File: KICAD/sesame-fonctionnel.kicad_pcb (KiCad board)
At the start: 2 copper layers, 1 part

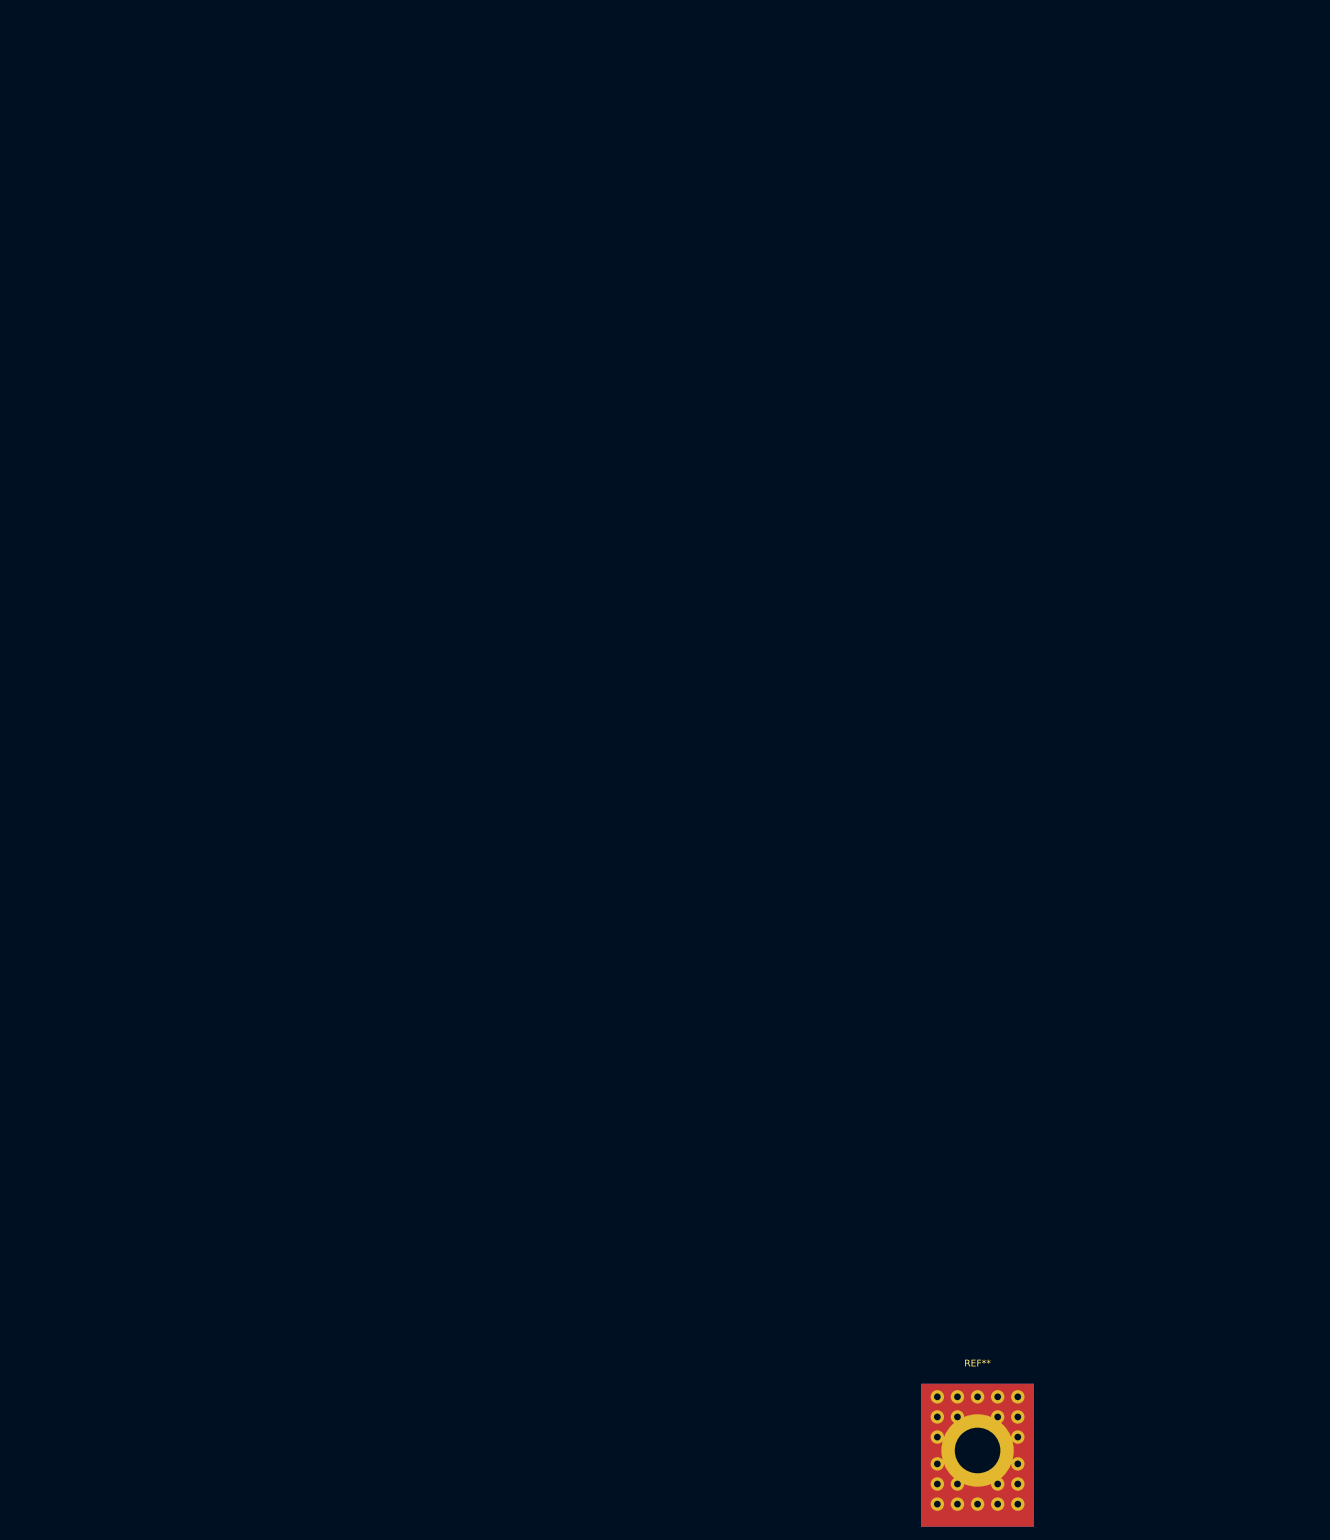
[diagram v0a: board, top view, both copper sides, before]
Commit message: edit footprints by jmt
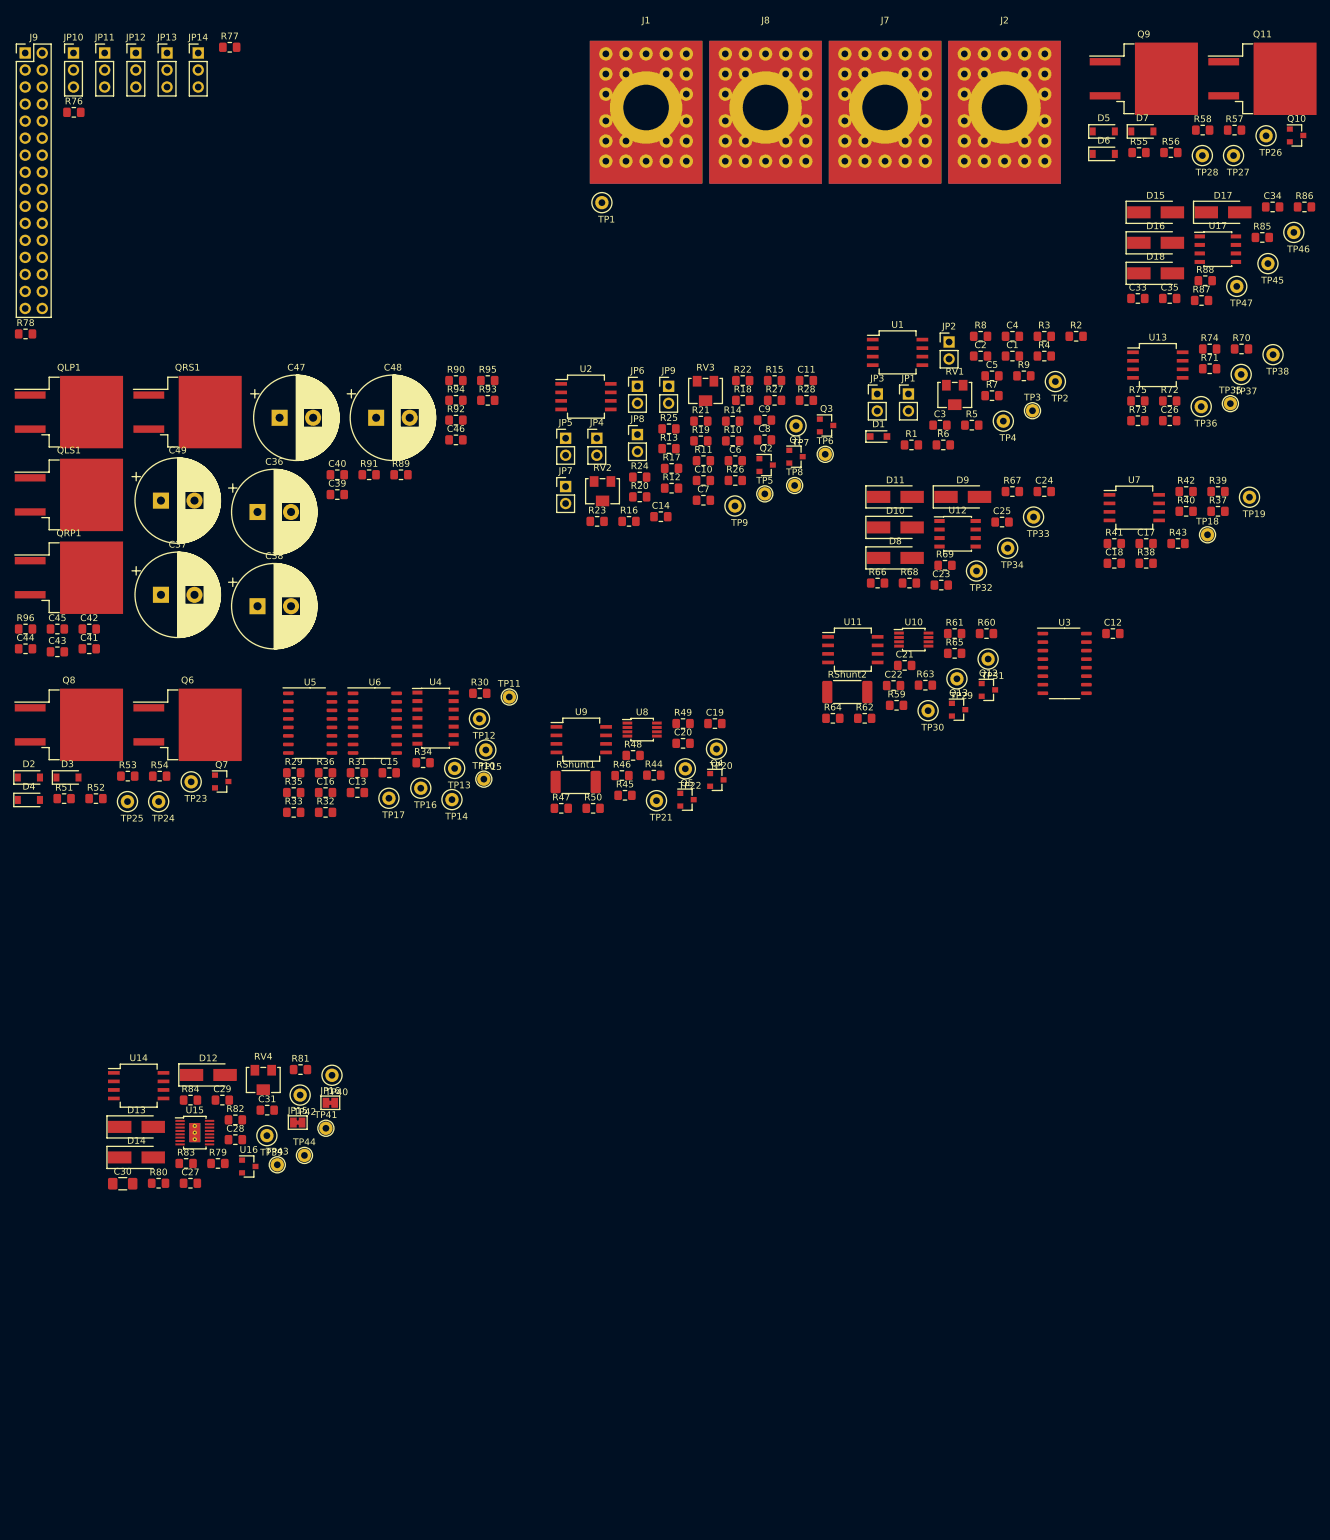
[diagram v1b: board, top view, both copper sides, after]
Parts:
- removed REF**: CXS70-14-C, Sesame_footprint:CXS70-14-C
- added C1: 100n, Capacitor_SMD:C_0805_2012Metric_Pad1.15x1.40mm_HandSolder, F.Cu at (160.8, -69.9)
- added C10: 10n, Capacitor_SMD:C_0805_2012Metric_Pad1.15x1.40mm_HandSolder, F.Cu at (114.7, -51.4)
- added C11: 10n, Capacitor_SMD:C_0805_2012Metric_Pad1.15x1.40mm_HandSolder, F.Cu at (130.1, -66.2)
- added C12: 100n, Capacitor_SMD:C_0805_2012Metric_Pad1.15x1.40mm_HandSolder, F.Cu at (175.8, -28.5)
- added C13: 100n, Capacitor_SMD:C_0805_2012Metric_Pad1.15x1.40mm_HandSolder, F.Cu at (63.1, -4.81)
- added C14: 100n, Capacitor_SMD:C_0805_2012Metric_Pad1.15x1.40mm_HandSolder, F.Cu at (108.4, -46.0)
- added C15: 100n, Capacitor_SMD:C_0805_2012Metric_Pad1.15x1.40mm_HandSolder, F.Cu at (67.9, -7.76)
- added C16: 100n, Capacitor_SMD:C_0805_2012Metric_Pad1.15x1.40mm_HandSolder, F.Cu at (58.4, -4.81)
- added C17: 100n, Capacitor_SMD:C_0805_2012Metric_Pad1.15x1.40mm_HandSolder, F.Cu at (180.7, -42.0)
- added C18: 2.2n, Capacitor_SMD:C_0805_2012Metric_Pad1.15x1.40mm_HandSolder, F.Cu at (176.0, -39.0)
- added C19: 100n, Capacitor_SMD:C_0805_2012Metric_Pad1.15x1.40mm_HandSolder, F.Cu at (116.4, -15.1)
- added C2: NC, Capacitor_SMD:C_0805_2012Metric_Pad1.15x1.40mm_HandSolder, F.Cu at (156.1, -69.9)
- added C20: 100n, Capacitor_SMD:C_0805_2012Metric_Pad1.15x1.40mm_HandSolder, F.Cu at (111.7, -12.2)
- added C21: 100n, Capacitor_SMD:C_0805_2012Metric_Pad1.15x1.40mm_HandSolder, F.Cu at (144.7, -23.8)
- added C22: 100n, Capacitor_SMD:C_0805_2012Metric_Pad1.15x1.40mm_HandSolder, F.Cu at (143.1, -20.8)
- added C23: 100n, Capacitor_SMD:C_0805_2012Metric_Pad1.15x1.40mm_HandSolder, F.Cu at (150.2, -35.8)
- added C24: 100n, Capacitor_SMD:C_0805_2012Metric_Pad1.15x1.40mm_HandSolder, F.Cu at (165.5, -49.7)
- added C25: 1u, Capacitor_SMD:C_0805_2012Metric_Pad1.15x1.40mm_HandSolder, F.Cu at (159.2, -45.1)
- added C26: 100n, Capacitor_SMD:C_0805_2012Metric_Pad1.15x1.40mm_HandSolder, F.Cu at (184.2, -60.3)
- added C27: 100n, Capacitor_SMD:C_0805_2012Metric_Pad1.15x1.40mm_HandSolder, F.Cu at (38.2, 53.5)
- added C28: C, Capacitor_SMD:C_0805_2012Metric_Pad1.15x1.40mm_HandSolder, F.Cu at (44.9, 47.0)
- added C29: C, Capacitor_SMD:C_0805_2012Metric_Pad1.15x1.40mm_HandSolder, F.Cu at (43.0, 41.0)
- added C3: 200n, Capacitor_SMD:C_0805_2012Metric_Pad1.15x1.40mm_HandSolder, F.Cu at (150.0, -59.6)
- added C30: 10u, Capacitor_SMD:C_1206_3216Metric_Pad1.42x1.75mm_HandSolder, F.Cu at (28.1, 53.5)
- added C31: C, Capacitor_SMD:C_0805_2012Metric_Pad1.15x1.40mm_HandSolder, F.Cu at (49.7, 42.5)
- added C33: 100n, Capacitor_SMD:C_0805_2012Metric_Pad1.15x1.40mm_HandSolder, F.Cu at (179.5, -78.5)
- added C34: 100n, Capacitor_SMD:C_0805_2012Metric_Pad1.15x1.40mm_HandSolder, F.Cu at (199.6, -92.1)
- added C35: 1u, Capacitor_SMD:C_0805_2012Metric_Pad1.15x1.40mm_HandSolder, F.Cu at (184.2, -78.5)
- added C36: 470uF, Capacitor_THT:CP_Radial_D12.5mm_P5.00mm, F.Cu at (48.2, -46.6)
- added C37: 470uF, Capacitor_THT:CP_Radial_D12.5mm_P5.00mm, F.Cu at (33.8, -34.3)
- added C38: 470uF, Capacitor_THT:CP_Radial_D12.5mm_P5.00mm, F.Cu at (48.2, -32.6)
- added C39: C, Capacitor_SMD:C_0805_2012Metric_Pad1.15x1.40mm_HandSolder, F.Cu at (60.1, -49.2)
- added C4: 22n, Capacitor_SMD:C_0805_2012Metric_Pad1.15x1.40mm_HandSolder, F.Cu at (160.8, -72.8)
- added C40: C, Capacitor_SMD:C_0805_2012Metric_Pad1.15x1.40mm_HandSolder, F.Cu at (60.1, -52.2)
- added C41: C, Capacitor_SMD:C_0805_2012Metric_Pad1.15x1.40mm_HandSolder, F.Cu at (23.1, -26.2)
- added C42: C, Capacitor_SMD:C_0805_2012Metric_Pad1.15x1.40mm_HandSolder, F.Cu at (23.1, -29.2)
- added C43: C, Capacitor_SMD:C_0805_2012Metric_Pad1.15x1.40mm_HandSolder, F.Cu at (18.4, -25.8)
- added C44: C, Capacitor_SMD:C_0805_2012Metric_Pad1.15x1.40mm_HandSolder, F.Cu at (13.6, -26.2)
- added C45: C, Capacitor_SMD:C_0805_2012Metric_Pad1.15x1.40mm_HandSolder, F.Cu at (18.4, -29.2)
- added C46: C, Capacitor_SMD:C_0805_2012Metric_Pad1.15x1.40mm_HandSolder, F.Cu at (77.8, -57.4)
- added C47: 470uF, Capacitor_THT:CP_Radial_D12.5mm_P5.00mm, F.Cu at (51.5, -60.7)
- added C48: 470uF, Capacitor_THT:CP_Radial_D12.5mm_P5.00mm, F.Cu at (65.9, -60.7)
- added C49: 470uF, Capacitor_THT:CP_Radial_D12.5mm_P5.00mm, F.Cu at (33.8, -48.4)
- added C5: 220n, Capacitor_SMD:C_0805_2012Metric_Pad1.15x1.40mm_HandSolder, F.Cu at (157.8, -67.0)
- added C6: 100n, Capacitor_SMD:C_0805_2012Metric_Pad1.15x1.40mm_HandSolder, F.Cu at (119.5, -54.3)
- added C7: 470n, Capacitor_SMD:C_0805_2012Metric_Pad1.15x1.40mm_HandSolder, F.Cu at (114.7, -48.4)
- added C8: 10n, Capacitor_SMD:C_0805_2012Metric_Pad1.15x1.40mm_HandSolder, F.Cu at (123.8, -57.4)
- added C9: 470n, Capacitor_SMD:C_0805_2012Metric_Pad1.15x1.40mm_HandSolder, F.Cu at (123.8, -60.4)
- added D1: BZX384B5V1, Diode_SMD:D_SOD-323_HandSoldering, F.Cu at (140.8, -57.9)
- added D10: SS36, Diode_SMD:D_SMA_Handsoldering, F.Cu at (143.3, -44.4)
- added D11: SS36, Diode_SMD:D_SMA_Handsoldering, F.Cu at (143.3, -48.9)
- added D12: SS36, Diode_SMD:D_SMA_Handsoldering, F.Cu at (40.9, 37.3)
- added D13: SS36, Diode_SMD:D_SMA_Handsoldering, F.Cu at (30.2, 45.0)
- added D14: SS36, Diode_SMD:D_SMA_Handsoldering, F.Cu at (30.2, 49.6)
- added D15: SS36, Diode_SMD:D_SMA_Handsoldering, F.Cu at (182.2, -91.3)
- added D16: SS36, Diode_SMD:D_SMA_Handsoldering, F.Cu at (182.2, -86.8)
- added D17: SS36, Diode_SMD:D_SMA_Handsoldering, F.Cu at (192.2, -91.3)
- added D18: SS36, Diode_SMD:D_SMA_Handsoldering, F.Cu at (182.2, -82.2)
- added D2: MMSZ5245, Diode_SMD:D_SOD-123, F.Cu at (14.1, -7.06)
- added D3: MMSZ5262, Diode_SMD:D_SOD-123, F.Cu at (19.9, -7.06)
- added D4: MMSZ5245, Diode_SMD:D_SOD-123, F.Cu at (14.1, -3.71)
- added D5: MMSZ5245, Diode_SMD:D_SOD-123, F.Cu at (174.4, -103.4)
- added D6: MMSZ5262, Diode_SMD:D_SOD-123, F.Cu at (174.4, -100.0)
- added D7: MMSZ5245, Diode_SMD:D_SOD-123, F.Cu at (180.2, -103.4)
- added D8: SS36, Diode_SMD:D_SMA_Handsoldering, F.Cu at (143.3, -39.8)
- added D9: SS36, Diode_SMD:D_SMA_Handsoldering, F.Cu at (153.4, -48.9)
- added J1: CXS70-14-C, Sesame_footprint:CXS70-14-C, F.Cu at (106.2, -107.0)
- added J2: CXS70-14-C, Sesame_footprint:CXS70-14-C, F.Cu at (159.6, -107.0)
- added J7: CXS70-14-C, Sesame_footprint:CXS70-14-C, F.Cu at (141.8, -107.0)
- added J8: CXS70-14-C, Sesame_footprint:CXS70-14-C, F.Cu at (124.0, -107.0)
- added J9: Conn_02x16_Odd_Even, Connector_PinHeader_2.54mm:PinHeader_2x16_P2.54mm_Vertical, F.Cu at (13.6, -115.1)
- added JP1: Jumper, Connector_PinHeader_2.54mm:PinHeader_1x02_P2.54mm_Vertical, F.Cu at (145.3, -64.2)
- added JP10: Jumper_NC_Dual, Connector_PinHeader_2.54mm:PinHeader_1x03_P2.54mm_Vertical, F.Cu at (20.8, -115.1)
- added JP11: Jumper_NC_Dual, Connector_PinHeader_2.54mm:PinHeader_1x03_P2.54mm_Vertical, F.Cu at (25.4, -115.1)
- added JP12: Jumper_NC_Dual, Connector_PinHeader_2.54mm:PinHeader_1x03_P2.54mm_Vertical, F.Cu at (30.1, -115.1)
- added JP13: Jumper_NC_Dual, Connector_PinHeader_2.54mm:PinHeader_1x03_P2.54mm_Vertical, F.Cu at (34.7, -115.1)
- added JP14: Jumper_NC_Dual, Connector_PinHeader_2.54mm:PinHeader_1x03_P2.54mm_Vertical, F.Cu at (39.4, -115.1)
- added JP15: Jumper_2_Bridged, Jumper:SolderJumper-2_P1.3mm_Bridged_Pad1.0x1.5mm, F.Cu at (54.2, 44.4)
- added JP16: Jumper_2_Bridged, Jumper:SolderJumper-2_P1.3mm_Bridged_Pad1.0x1.5mm, F.Cu at (59.1, 41.5)
- added JP2: Jumper, Connector_PinHeader_2.54mm:PinHeader_1x02_P2.54mm_Vertical, F.Cu at (151.3, -72.0)
- added JP3: Jumper, Connector_PinHeader_2.54mm:PinHeader_1x02_P2.54mm_Vertical, F.Cu at (140.6, -64.2)
- added JP4: Jumper, Connector_PinHeader_2.54mm:PinHeader_1x02_P2.54mm_Vertical, F.Cu at (98.8, -57.6)
- added JP5: Jumper, Connector_PinHeader_2.54mm:PinHeader_1x02_P2.54mm_Vertical, F.Cu at (94.2, -57.6)
- added JP6: Jumper, Connector_PinHeader_2.54mm:PinHeader_1x02_P2.54mm_Vertical, F.Cu at (104.9, -65.4)
- added JP7: Jumper, Connector_PinHeader_2.54mm:PinHeader_1x02_P2.54mm_Vertical, F.Cu at (94.2, -50.5)
- added JP8: Jumper, Connector_PinHeader_2.54mm:PinHeader_1x02_P2.54mm_Vertical, F.Cu at (104.9, -58.2)
- added JP9: Jumper, Connector_PinHeader_2.54mm:PinHeader_1x02_P2.54mm_Vertical, F.Cu at (109.5, -65.4)
- added Q1: BC847, Package_TO_SOT_SMD:SOT-23, F.Cu at (128.5, -54.9)
- added Q10: BC857, Package_TO_SOT_SMD:SOT-23, F.Cu at (203.2, -102.8)
- added Q11: SQM120, Package_TO_SOT_SMD:TO-263-2, F.Cu at (198.1, -111.2)
- added Q12: BC847, Package_TO_SOT_SMD:SOT-23, F.Cu at (157.2, -20.1)
- added Q13: BC847, Package_TO_SOT_SMD:SOT-23, F.Cu at (152.8, -17.2)
- added Q2: BC847, Package_TO_SOT_SMD:SOT-23, F.Cu at (124.1, -53.6)
- added Q3: BC847, Package_TO_SOT_SMD:SOT-23, F.Cu at (133.1, -59.5)
- added Q4: BC847, Package_TO_SOT_SMD:SOT-23, F.Cu at (116.7, -6.70)
- added Q5: BC847, Package_TO_SOT_SMD:SOT-23, F.Cu at (112.3, -3.75)
- added Q6: SQM120, Package_TO_SOT_SMD:TO-263-2, F.Cu at (37.8, -14.9)
- added Q7: BC857, Package_TO_SOT_SMD:SOT-23, F.Cu at (42.9, -6.46)
- added Q8: SQM120, Package_TO_SOT_SMD:TO-263-2, F.Cu at (20.1, -14.9)
- added Q9: SQM120, Package_TO_SOT_SMD:TO-263-2, F.Cu at (180.4, -111.2)
- added QLP1: TK65G10N1, Package_TO_SOT_SMD:TO-263-2, F.Cu at (20.1, -61.5)
- added QLS1: TK65G10N1, Package_TO_SOT_SMD:TO-263-2, F.Cu at (20.1, -49.2)
- added QRP1: TK65G10N1, Package_TO_SOT_SMD:TO-263-2, F.Cu at (20.1, -36.9)
- added QRS1: TK65G10N1, Package_TO_SOT_SMD:TO-263-2, F.Cu at (37.8, -61.5)
- added R1: 10k, Resistor_SMD:R_0805_2012Metric_Pad1.15x1.40mm_HandSolder, F.Cu at (145.7, -56.6)
- added R10: R, Resistor_SMD:R_0805_2012Metric_Pad1.15x1.40mm_HandSolder, F.Cu at (119.1, -57.2)
- added R11: R, Resistor_SMD:R_0805_2012Metric_Pad1.15x1.40mm_HandSolder, F.Cu at (114.7, -54.3)
- added R12: R, Resistor_SMD:R_0805_2012Metric_Pad1.15x1.40mm_HandSolder, F.Cu at (110.0, -50.2)
- added R13: R, Resistor_SMD:R_0805_2012Metric_Pad1.15x1.40mm_HandSolder, F.Cu at (109.6, -56.1)
- added R14: 100k, Resistor_SMD:R_0805_2012Metric_Pad1.15x1.40mm_HandSolder, F.Cu at (119.1, -60.2)
- added R15: 100k, Resistor_SMD:R_0805_2012Metric_Pad1.15x1.40mm_HandSolder, F.Cu at (125.3, -66.2)
- added R16: 100k, Resistor_SMD:R_0805_2012Metric_Pad1.15x1.40mm_HandSolder, F.Cu at (103.6, -45.2)
- added R17: 100k, Resistor_SMD:R_0805_2012Metric_Pad1.15x1.40mm_HandSolder, F.Cu at (110.0, -53.1)
- added R18: 100k, Resistor_SMD:R_0805_2012Metric_Pad1.15x1.40mm_HandSolder, F.Cu at (120.6, -63.3)
- added R19: 100k, Resistor_SMD:R_0805_2012Metric_Pad1.15x1.40mm_HandSolder, F.Cu at (114.3, -57.2)
- added R2: 10k, Resistor_SMD:R_0805_2012Metric_Pad1.15x1.40mm_HandSolder, F.Cu at (170.3, -72.8)
- added R20: 100k, Resistor_SMD:R_0805_2012Metric_Pad1.15x1.40mm_HandSolder, F.Cu at (105.2, -48.9)
- added R21: 100k, Resistor_SMD:R_0805_2012Metric_Pad1.15x1.40mm_HandSolder, F.Cu at (114.3, -60.2)
- added R22: 47k, Resistor_SMD:R_0805_2012Metric_Pad1.15x1.40mm_HandSolder, F.Cu at (120.6, -66.2)
- added R23: 47k, Resistor_SMD:R_0805_2012Metric_Pad1.15x1.40mm_HandSolder, F.Cu at (98.9, -45.2)
- added R24: 47k, Resistor_SMD:R_0805_2012Metric_Pad1.15x1.40mm_HandSolder, F.Cu at (105.2, -51.9)
- added R25: 47k, Resistor_SMD:R_0805_2012Metric_Pad1.15x1.40mm_HandSolder, F.Cu at (109.6, -59.0)
- added R26: 10k, Resistor_SMD:R_0805_2012Metric_Pad1.15x1.40mm_HandSolder, F.Cu at (119.5, -51.4)
- added R27: 47k, Resistor_SMD:R_0805_2012Metric_Pad1.15x1.40mm_HandSolder, F.Cu at (125.3, -63.3)
- added R28: 1k, Resistor_SMD:R_0805_2012Metric_Pad1.15x1.40mm_HandSolder, F.Cu at (130.1, -63.3)
- added R29: 10k, Resistor_SMD:R_0805_2012Metric_Pad1.15x1.40mm_HandSolder, F.Cu at (53.6, -7.76)
- added R3: 10k, Resistor_SMD:R_0805_2012Metric_Pad1.15x1.40mm_HandSolder, F.Cu at (165.6, -72.8)
- added R30: 10k, Resistor_SMD:R_0805_2012Metric_Pad1.15x1.40mm_HandSolder, F.Cu at (81.4, -19.6)
- added R31: 10k, Resistor_SMD:R_0805_2012Metric_Pad1.15x1.40mm_HandSolder, F.Cu at (63.1, -7.76)
- added R32: 10k, Resistor_SMD:R_0805_2012Metric_Pad1.15x1.40mm_HandSolder, F.Cu at (58.4, -1.86)
- added R33: NC, Resistor_SMD:R_0805_2012Metric_Pad1.15x1.40mm_HandSolder, F.Cu at (53.6, -1.86)
- added R34: NC, Resistor_SMD:R_0805_2012Metric_Pad1.15x1.40mm_HandSolder, F.Cu at (72.9, -9.26)
- added R35: 10k, Resistor_SMD:R_0805_2012Metric_Pad1.15x1.40mm_HandSolder, F.Cu at (53.6, -4.81)
- added R36: 10k, Resistor_SMD:R_0805_2012Metric_Pad1.15x1.40mm_HandSolder, F.Cu at (58.4, -7.76)
- added R37: 10k, Resistor_SMD:R_0805_2012Metric_Pad1.15x1.40mm_HandSolder, F.Cu at (191.4, -46.8)
- added R38: 11k, Resistor_SMD:R_0805_2012Metric_Pad1.15x1.40mm_HandSolder, F.Cu at (180.7, -39.0)
- added R39: 6.8k, Resistor_SMD:R_0805_2012Metric_Pad1.15x1.40mm_HandSolder, F.Cu at (191.4, -49.7)
- added R4: 10k, Resistor_SMD:R_0805_2012Metric_Pad1.15x1.40mm_HandSolder, F.Cu at (165.6, -69.9)
- added R40: 10k, Resistor_SMD:R_0805_2012Metric_Pad1.15x1.40mm_HandSolder, F.Cu at (186.7, -46.8)
- added R41: 13k, Resistor_SMD:R_0805_2012Metric_Pad1.15x1.40mm_HandSolder, F.Cu at (176.0, -42.0)
- added R42: 18k, Resistor_SMD:R_0805_2012Metric_Pad1.15x1.40mm_HandSolder, F.Cu at (186.7, -49.7)
- added R43: 680, Resistor_SMD:R_0805_2012Metric_Pad1.15x1.40mm_HandSolder, F.Cu at (185.5, -42.0)
- added R44: 200, Resistor_SMD:R_0805_2012Metric_Pad1.15x1.40mm_HandSolder, F.Cu at (107.3, -7.40)
- added R45: 200, Resistor_SMD:R_0805_2012Metric_Pad1.15x1.40mm_HandSolder, F.Cu at (103.0, -4.40)
- added R46: 200, Resistor_SMD:R_0805_2012Metric_Pad1.15x1.40mm_HandSolder, F.Cu at (102.6, -7.35)
- added R47: 200, Resistor_SMD:R_0805_2012Metric_Pad1.15x1.40mm_HandSolder, F.Cu at (93.5, -2.46)
- added R48: 20k, Resistor_SMD:R_0805_2012Metric_Pad1.15x1.40mm_HandSolder, F.Cu at (104.2, -10.3)
- added R49: 90k, Resistor_SMD:R_0805_2012Metric_Pad1.15x1.40mm_HandSolder, F.Cu at (111.7, -15.1)
- added R5: 10k, Resistor_SMD:R_0805_2012Metric_Pad1.15x1.40mm_HandSolder, F.Cu at (154.7, -59.6)
- added R50: 10k, Resistor_SMD:R_0805_2012Metric_Pad1.15x1.40mm_HandSolder, F.Cu at (98.3, -2.46)
- added R51: 330k, Resistor_SMD:R_0805_2012Metric_Pad1.15x1.40mm_HandSolder, F.Cu at (19.4, -3.91)
- added R52: 100k, Resistor_SMD:R_0805_2012Metric_Pad1.15x1.40mm_HandSolder, F.Cu at (24.1, -3.91)
- added R53: 100k, Resistor_SMD:R_0805_2012Metric_Pad1.15x1.40mm_HandSolder, F.Cu at (28.9, -7.26)
- added R54: 1M, Resistor_SMD:R_0805_2012Metric_Pad1.15x1.40mm_HandSolder, F.Cu at (33.6, -7.26)
- added R55: 330k, Resistor_SMD:R_0805_2012Metric_Pad1.15x1.40mm_HandSolder, F.Cu at (179.7, -100.2)
- added R56: 100k, Resistor_SMD:R_0805_2012Metric_Pad1.15x1.40mm_HandSolder, F.Cu at (184.4, -100.2)
- added R57: 100k, Resistor_SMD:R_0805_2012Metric_Pad1.15x1.40mm_HandSolder, F.Cu at (193.9, -103.6)
- added R58: 1M, Resistor_SMD:R_0805_2012Metric_Pad1.15x1.40mm_HandSolder, F.Cu at (189.2, -103.6)
- added R59: 200, Resistor_SMD:R_0805_2012Metric_Pad1.15x1.40mm_HandSolder, F.Cu at (143.5, -17.8)
- added R6: NC, Resistor_SMD:R_0805_2012Metric_Pad1.15x1.40mm_HandSolder, F.Cu at (150.5, -56.6)
- added R60: 200, Resistor_SMD:R_0805_2012Metric_Pad1.15x1.40mm_HandSolder, F.Cu at (156.9, -28.5)
- added R61: 200, Resistor_SMD:R_0805_2012Metric_Pad1.15x1.40mm_HandSolder, F.Cu at (152.2, -28.5)
- added R62: 200, Resistor_SMD:R_0805_2012Metric_Pad1.15x1.40mm_HandSolder, F.Cu at (138.8, -15.9)
- added R63: 20k, Resistor_SMD:R_0805_2012Metric_Pad1.15x1.40mm_HandSolder, F.Cu at (147.8, -20.8)
- added R64: 90k, Resistor_SMD:R_0805_2012Metric_Pad1.15x1.40mm_HandSolder, F.Cu at (134.0, -15.9)
- added R65: 10k, Resistor_SMD:R_0805_2012Metric_Pad1.15x1.40mm_HandSolder, F.Cu at (152.2, -25.6)
- added R66: 1, Resistor_SMD:R_0805_2012Metric_Pad1.15x1.40mm_HandSolder, F.Cu at (140.7, -36.0)
- added R67: 1, Resistor_SMD:R_0805_2012Metric_Pad1.15x1.40mm_HandSolder, F.Cu at (160.8, -49.7)
- added R68: 5, Resistor_SMD:R_0805_2012Metric_Pad1.15x1.40mm_HandSolder, F.Cu at (145.4, -36.0)
- added R69: 5, Resistor_SMD:R_0805_2012Metric_Pad1.15x1.40mm_HandSolder, F.Cu at (150.7, -38.7)
- added R7: 10k, Resistor_SMD:R_0805_2012Metric_Pad1.15x1.40mm_HandSolder, F.Cu at (157.8, -64.0)
- added R70: 100k, Resistor_SMD:R_0805_2012Metric_Pad1.15x1.40mm_HandSolder, F.Cu at (195.0, -71.0)
- added R71: 4.7k, Resistor_SMD:R_0805_2012Metric_Pad1.15x1.40mm_HandSolder, F.Cu at (190.2, -68.0)
- added R72: 100k, Resistor_SMD:R_0805_2012Metric_Pad1.15x1.40mm_HandSolder, F.Cu at (184.2, -63.2)
- added R73: 100k, Resistor_SMD:R_0805_2012Metric_Pad1.15x1.40mm_HandSolder, F.Cu at (179.5, -60.3)
- added R74: 100k, Resistor_SMD:R_0805_2012Metric_Pad1.15x1.40mm_HandSolder, F.Cu at (190.2, -71.0)
- added R75: 100k, Resistor_SMD:R_0805_2012Metric_Pad1.15x1.40mm_HandSolder, F.Cu at (179.5, -63.2)
- added R76: 10k, Resistor_SMD:R_0805_2012Metric_Pad1.15x1.40mm_HandSolder, F.Cu at (20.8, -106.2)
- added R77: 10k, Resistor_SMD:R_0805_2012Metric_Pad1.15x1.40mm_HandSolder, F.Cu at (44.1, -116.0)
- added R78: 10k, Resistor_SMD:R_0805_2012Metric_Pad1.15x1.40mm_HandSolder, F.Cu at (13.6, -73.2)
- added R79: 84.5, Resistor_SMD:R_0805_2012Metric_Pad1.15x1.40mm_HandSolder, F.Cu at (42.3, 50.5)
- added R8: 20k, Resistor_SMD:R_0805_2012Metric_Pad1.15x1.40mm_HandSolder, F.Cu at (156.1, -72.8)
- added R80: R, Resistor_SMD:R_0805_2012Metric_Pad1.15x1.40mm_HandSolder, F.Cu at (33.5, 53.5)
- added R81: 1M, Resistor_SMD:R_0805_2012Metric_Pad1.15x1.40mm_HandSolder, F.Cu at (54.6, 36.5)
- added R82: 296k, Resistor_SMD:R_0805_2012Metric_Pad1.15x1.40mm_HandSolder, F.Cu at (44.9, 44.0)
- added R83: R, Resistor_SMD:R_0805_2012Metric_Pad1.15x1.40mm_HandSolder, F.Cu at (37.6, 50.5)
- added R84: 10k, Resistor_SMD:R_0805_2012Metric_Pad1.15x1.40mm_HandSolder, F.Cu at (38.2, 41.0)
- added R85: 1, Resistor_SMD:R_0805_2012Metric_Pad1.15x1.40mm_HandSolder, F.Cu at (198.1, -87.6)
- added R86: 1, Resistor_SMD:R_0805_2012Metric_Pad1.15x1.40mm_HandSolder, F.Cu at (204.3, -92.1)
- added R87: 5, Resistor_SMD:R_0805_2012Metric_Pad1.15x1.40mm_HandSolder, F.Cu at (189.0, -78.2)
- added R88: 5, Resistor_SMD:R_0805_2012Metric_Pad1.15x1.40mm_HandSolder, F.Cu at (189.6, -81.1)
- added R89: R, Resistor_SMD:R_0805_2012Metric_Pad1.15x1.40mm_HandSolder, F.Cu at (69.6, -52.2)
- added R9: 390, Resistor_SMD:R_0805_2012Metric_Pad1.15x1.40mm_HandSolder, F.Cu at (162.5, -67.0)
- added R90: R, Resistor_SMD:R_0805_2012Metric_Pad1.15x1.40mm_HandSolder, F.Cu at (77.8, -66.2)
- added R91: R, Resistor_SMD:R_0805_2012Metric_Pad1.15x1.40mm_HandSolder, F.Cu at (64.9, -52.2)
- added R92: R, Resistor_SMD:R_0805_2012Metric_Pad1.15x1.40mm_HandSolder, F.Cu at (77.8, -60.4)
- added R93: R, Resistor_SMD:R_0805_2012Metric_Pad1.15x1.40mm_HandSolder, F.Cu at (82.6, -63.3)
- added R94: R, Resistor_SMD:R_0805_2012Metric_Pad1.15x1.40mm_HandSolder, F.Cu at (77.8, -63.3)
- added R95: R, Resistor_SMD:R_0805_2012Metric_Pad1.15x1.40mm_HandSolder, F.Cu at (82.6, -66.2)
- added R96: R, Resistor_SMD:R_0805_2012Metric_Pad1.15x1.40mm_HandSolder, F.Cu at (13.6, -29.2)
- added RShunt1: PA2512FKF070R005E, Resistor_SMD:R_2512_6332Metric_Pad1.52x3.35mm_HandSolder, F.Cu at (95.7, -6.38)
- added RShunt2: PA2512FKF070R005E, Resistor_SMD:R_2512_6332Metric_Pad1.52x3.35mm_HandSolder, F.Cu at (136.2, -19.8)
- added RV1: 10K, Potentiometer_SMD:Potentiometer_Bourns_3214W_Vertical, F.Cu at (152.2, -64.1)
- added RV2: 10K, Potentiometer_SMD:Potentiometer_Bourns_3214W_Vertical, F.Cu at (99.7, -49.8)
- added RV3: 10K, Potentiometer_SMD:Potentiometer_Bourns_3214W_Vertical, F.Cu at (115.0, -64.7)
- added RV4: 10K, Potentiometer_SMD:Potentiometer_Bourns_3214W_Vertical, F.Cu at (49.1, 38.0)
- added TP1: TP_POP, TestPoint:TestPoint_Loop_D1.80mm_Drill1.0mm_Beaded, F.Cu at (99.6, -92.8)
- added TP10: TP_NOP, TestPoint:TestPoint_THTPad_D2.0mm_Drill1.0mm, F.Cu at (82.0, -6.81)
- added TP11: TP_NOP, TestPoint:TestPoint_THTPad_D2.0mm_Drill1.0mm, F.Cu at (85.8, -19.1)
- added TP12: TP_POP, TestPoint:TestPoint_Loop_D1.80mm_Drill1.0mm_Beaded, F.Cu at (81.3, -15.8)
- added TP13: TP_POP, TestPoint:TestPoint_Loop_D1.80mm_Drill1.0mm_Beaded, F.Cu at (77.6, -8.41)
- added TP14: TP_POP, TestPoint:TestPoint_Loop_D1.80mm_Drill1.0mm_Beaded, F.Cu at (77.2, -3.76)
- added TP15: TP_POP, TestPoint:TestPoint_Loop_D1.80mm_Drill1.0mm_Beaded, F.Cu at (82.3, -11.2)
- added TP16: TP_POP, TestPoint:TestPoint_Loop_D1.80mm_Drill1.0mm_Beaded, F.Cu at (72.6, -5.46)
- added TP17: TP_POP, TestPoint:TestPoint_Loop_D1.80mm_Drill1.0mm_Beaded, F.Cu at (67.8, -3.96)
- added TP18: TP_NOP, TestPoint:TestPoint_THTPad_D2.0mm_Drill1.0mm, F.Cu at (189.9, -43.2)
- added TP19: TP_POP, TestPoint:TestPoint_Loop_D1.80mm_Drill1.0mm_Beaded, F.Cu at (196.2, -48.9)
- added TP2: TP_POP, TestPoint:TestPoint_Loop_D1.80mm_Drill1.0mm_Beaded, F.Cu at (167.2, -66.1)
- added TP20: TP_POP, TestPoint:TestPoint_Loop_D1.80mm_Drill1.0mm_Beaded, F.Cu at (116.7, -11.3)
- added TP21: TP_POP, TestPoint:TestPoint_Loop_D1.80mm_Drill1.0mm_Beaded, F.Cu at (107.7, -3.60)
- added TP22: TP_POP, TestPoint:TestPoint_Loop_D1.80mm_Drill1.0mm_Beaded, F.Cu at (112.0, -8.35)
- added TP23: TP_POP, TestPoint:TestPoint_Loop_D1.80mm_Drill1.0mm_Beaded, F.Cu at (38.3, -6.41)
- added TP24: TP_POP, TestPoint:TestPoint_Loop_D1.80mm_Drill1.0mm_Beaded, F.Cu at (33.5, -3.46)
- added TP25: TP_POP, TestPoint:TestPoint_Loop_D1.80mm_Drill1.0mm_Beaded, F.Cu at (28.8, -3.46)
- added TP26: TP_POP, TestPoint:TestPoint_Loop_D1.80mm_Drill1.0mm_Beaded, F.Cu at (198.6, -102.8)
- added TP27: TP_POP, TestPoint:TestPoint_Loop_D1.80mm_Drill1.0mm_Beaded, F.Cu at (193.8, -99.8)
- added TP28: TP_POP, TestPoint:TestPoint_Loop_D1.80mm_Drill1.0mm_Beaded, F.Cu at (189.1, -99.8)
- added TP29: TP_POP, TestPoint:TestPoint_Loop_D1.80mm_Drill1.0mm_Beaded, F.Cu at (152.5, -21.8)
- added TP3: TP_NOP, TestPoint:TestPoint_THTPad_D2.0mm_Drill1.0mm, F.Cu at (163.8, -61.8)
- added TP30: TP_POP, TestPoint:TestPoint_Loop_D1.80mm_Drill1.0mm_Beaded, F.Cu at (148.2, -17.0)
- added TP31: TP_POP, TestPoint:TestPoint_Loop_D1.80mm_Drill1.0mm_Beaded, F.Cu at (157.2, -24.7)
- added TP32: TP_POP, TestPoint:TestPoint_Loop_D1.80mm_Drill1.0mm_Beaded, F.Cu at (155.4, -37.9)
- added TP33: TP_POP, TestPoint:TestPoint_Loop_D1.80mm_Drill1.0mm_Beaded, F.Cu at (163.9, -45.9)
- added TP34: TP_POP, TestPoint:TestPoint_Loop_D1.80mm_Drill1.0mm_Beaded, F.Cu at (160.1, -41.2)
- added TP35: TP_NOP, TestPoint:TestPoint_THTPad_D2.0mm_Drill1.0mm, F.Cu at (193.3, -62.8)
- added TP36: TP_POP, TestPoint:TestPoint_Loop_D1.80mm_Drill1.0mm_Beaded, F.Cu at (188.9, -62.4)
- added TP37: TP_POP, TestPoint:TestPoint_Loop_D1.80mm_Drill1.0mm_Beaded, F.Cu at (194.9, -67.2)
- added TP38: TP_POP, TestPoint:TestPoint_Loop_D1.80mm_Drill1.0mm_Beaded, F.Cu at (199.7, -70.1)
- added TP39: TP_POP, TestPoint:TestPoint_Loop_D1.80mm_Drill1.0mm_Beaded, F.Cu at (49.6, 46.4)
- added TP4: TP_POP, TestPoint:TestPoint_Loop_D1.80mm_Drill1.0mm_Beaded, F.Cu at (159.4, -60.2)
- added TP40: TP_POP, TestPoint:TestPoint_Loop_D1.80mm_Drill1.0mm_Beaded, F.Cu at (59.3, 37.4)
- added TP41: TP_NOP, TestPoint:TestPoint_THTPad_D2.0mm_Drill1.0mm, F.Cu at (58.4, 45.2)
- added TP42: TP_POP, TestPoint:TestPoint_Loop_D1.80mm_Drill1.0mm_Beaded, F.Cu at (54.6, 40.3)
- added TP43: TP_NOP, TestPoint:TestPoint_THTPad_D2.0mm_Drill1.0mm, F.Cu at (51.2, 50.7)
- added TP44: TP_NOP, TestPoint:TestPoint_THTPad_D2.0mm_Drill1.0mm, F.Cu at (55.2, 49.3)
- added TP45: TP_POP, TestPoint:TestPoint_Loop_D1.80mm_Drill1.0mm_Beaded, F.Cu at (198.9, -83.7)
- added TP46: TP_POP, TestPoint:TestPoint_Loop_D1.80mm_Drill1.0mm_Beaded, F.Cu at (202.8, -88.3)
- added TP47: TP_POP, TestPoint:TestPoint_Loop_D1.80mm_Drill1.0mm_Beaded, F.Cu at (194.2, -80.3)
- added TP5: TP_NOP, TestPoint:TestPoint_THTPad_D2.0mm_Drill1.0mm, F.Cu at (123.9, -49.4)
- added TP6: TP_NOP, TestPoint:TestPoint_THTPad_D2.0mm_Drill1.0mm, F.Cu at (132.9, -55.2)
- added TP7: TP_POP, TestPoint:TestPoint_Loop_D1.80mm_Drill1.0mm_Beaded, F.Cu at (128.5, -59.5)
- added TP8: TP_NOP, TestPoint:TestPoint_THTPad_D2.0mm_Drill1.0mm, F.Cu at (128.3, -50.6)
- added TP9: TP_POP, TestPoint:TestPoint_Loop_D1.80mm_Drill1.0mm_Beaded, F.Cu at (119.4, -47.5)
- added U1: AD8030, Package_SO:SO-8_5.3x6.2mm_P1.27mm, F.Cu at (143.7, -70.5)
- added U10: LT6016, Package_SO:MSOP-8_3x3mm_P0.65mm, F.Cu at (146.1, -27.6)
- added U11: AD8030, Package_SO:SO-8_5.3x6.2mm_P1.27mm, F.Cu at (137.0, -26.1)
- added U12: UCC27284-Q1, Package_SO:SOIC-8_3.9x4.9mm_P1.27mm, F.Cu at (152.6, -43.4)
- added U13: AD8030, Package_SO:SO-8_5.3x6.2mm_P1.27mm, F.Cu at (182.5, -68.6)
- added U14: AD8030, Package_SO:SO-8_5.3x6.2mm_P1.27mm, F.Cu at (30.5, 38.9)
- added U15: LT8365, Package_SO:MSOP-16-1EP_3x4mm_P0.5mm_EP1.65x2.85mm_ThermalVias, F.Cu at (38.9, 45.9)
- added U16: LM4040DBZ-2.5, Package_TO_SOT_SMD:SOT-23, F.Cu at (46.9, 51.0)
- added U17: UCC27284-Q1, Package_SO:SOIC-8_3.9x4.9mm_P1.27mm, F.Cu at (191.4, -85.8)
- added U2: LM2903, Package_SO:SO-8_5.3x6.2mm_P1.27mm, F.Cu at (97.2, -63.9)
- added U3: CD4053BM96, Package_SO:SOIC-16_4.55x10.3mm_P1.27mm, F.Cu at (168.6, -24.1)
- added U4: 4011, Package_SO:SOIC-14_3.9x8.7mm_P1.27mm, F.Cu at (74.8, -15.9)
- added U5: CD4053BM96, Package_SO:SOIC-16_4.55x10.3mm_P1.27mm, F.Cu at (56.1, -15.2)
- added U6: CD4053BM96, Package_SO:SOIC-16_4.55x10.3mm_P1.27mm, F.Cu at (65.7, -15.2)
- added U7: AD8030, Package_SO:SO-8_5.3x6.2mm_P1.27mm, F.Cu at (179.0, -47.3)
- added U8: LT6016, Package_SO:MSOP-8_3x3mm_P0.65mm, F.Cu at (105.6, -14.2)
- added U9: AD8030, Package_SO:SO-8_5.3x6.2mm_P1.27mm, F.Cu at (96.5, -12.7)

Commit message: route + work on djd
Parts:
- removed R27: 47k, Resistor_SMD:R_0805_2012Metric_Pad1.15x1.40mm_HandSolder
- removed R28: 1k, Resistor_SMD:R_0805_2012Metric_Pad1.15x1.40mm_HandSolder
- added H1: MountingHole, MountingHole:MountingHole_3.2mm_M3, F.Cu at (235.0, 65.0)
- added H2: MountingHole, MountingHole:MountingHole_3.2mm_M3, F.Cu at (235.0, 155.0)
- added H3: MountingHole, MountingHole:MountingHole_3.2mm_M3, F.Cu at (85.0, 155.0)
- added H4: MountingHole, MountingHole:MountingHole_3.2mm_M3, F.Cu at (85.0, 65.0)
- added L2: INDUCTOR, Sesame_footprint:Multi-coil, F.Cu at (195.6, 110.0)
- C14: value 100n -> 470n
- C3: value 200n -> 470n
- R3, R4, R5: value 10k -> 47k
- moved QRP1 326.9 mm to (319.3, 94.8)
- moved QLP1 320.8 mm to (300.4, 94.6), turned to 180 degrees
- moved QRS1 315.9 mm to (319.2, 81.9)
- moved QLS1 309.6 mm to (300.6, 81.9), turned to 180 degrees
- moved C41 304.7 mm to (314.0, 64.6)
- moved C42 304.7 mm to (314.0, 61.6)
- moved C43 304.7 mm to (309.2, 65.0)
- moved C44 304.7 mm to (304.5, 64.6)
- moved C45 304.7 mm to (309.2, 61.6)
- moved R96 304.7 mm to (304.5, 61.6)
- moved TP1 299.7 mm to (282.9, 144.4)
- moved C39 286.3 mm to (321.7, 67.0)
- moved C40 286.3 mm to (321.7, 64.0)
- moved C46 286.3 mm to (339.4, 58.8)
- moved R89 286.3 mm to (331.2, 64.0)
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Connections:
- net /LEFT PROTECTION/IO_PWR renamed /L
- net /RIGHT PROTECTION/IO_PWR renamed /R
- JP10 pad 1: (no net) -> /INT_PWM_Power
- JP10 pad 2: (no net) -> /PWM
- JP11 pad 1: (no net) -> /~INT_PWM_Freewheel
- JP11 pad 2: (no net) -> /~PWM
- Q1 pad 1: Net-(Q1-Pad1) -> /Rearm
- Q1 pad 3: Net-(C11-Pad1) -> Net-(Q1-Pad3)
- Q2 pad 1: /Rearm -> /PROGRAMMABLE BREAKER/S
- Q2 pad 3: Net-(Q2-Pad3) -> Net-(C11-Pad1)
- Q3 pad 2: GND -> /~Over_UI_Protection
- Q3 pad 3: Net-(Q3-Pad3) -> VCC
- R22 pad 2: Net-(C11-Pad1) -> Net-(Q1-Pad3)
- R23 pad 1: Net-(C11-Pad1) -> Net-(Q1-Pad3)
- R23 pad 2: /Rearm -> /PROGRAMMABLE BREAKER/S
- R24 pad 1: Net-(Q1-Pad1) -> /Rearm
- R24 pad 2: Net-(Q2-Pad3) -> Net-(C11-Pad1)
- R25 pad 2: Net-(Q2-Pad3) -> Net-(C11-Pad1)
- R26 pad 2: Net-(Q2-Pad3) -> Net-(C11-Pad1)
- R44 pad 2: /VProt_Left -> /DC/DC CONVERTER/VD_LS
- R45 pad 2: /DC/DC CONVERTER/VD_LS -> /VProt_Left
- R46 pad 2: /DC/DC CONVERTER/VD_LS -> /VProt_Left
- R47 pad 2: /VProt_Left -> /DC/DC CONVERTER/VD_LS
- R49 pad 1: /DC/DC CONVERTER/VD_LS -> /VProt_Left
- R59 pad 2: /VProt_Right -> /U/I SENSOR RIGHT/VD_Mos
- R60 pad 2: /U/I SENSOR RIGHT/VD_Mos -> /VProt_Right
- R61 pad 2: /U/I SENSOR RIGHT/VD_Mos -> /VProt_Right
- R62 pad 2: /VProt_Right -> /U/I SENSOR RIGHT/VD_Mos
- R64 pad 1: /U/I SENSOR RIGHT/VD_Mos -> /VProt_Right
- RShunt1 pad 1: /DC/DC CONVERTER/VD_LS -> /VProt_Left
- RShunt1 pad 2: /VProt_Left -> /DC/DC CONVERTER/VD_LS
- RShunt2 pad 1: /U/I SENSOR RIGHT/VD_Mos -> /VProt_Right
- RShunt2 pad 2: /VProt_Right -> /U/I SENSOR RIGHT/VD_Mos
- TP37 pad 1: /PWM GEN/~PWM_FREEWHEEL -> /~INT_PWM_Freewheel
- TP38 pad 1: /PWM GEN/PWM_POWER -> /INT_PWM_Power
- TP7 pad 1: Net-(Q1-Pad1) -> /PROGRAMMABLE BREAKER/S
- TP8 pad 1: Net-(Q2-Pad3) -> Net-(C11-Pad1)
- TP9 pad 1: Net-(Q3-Pad3) -> /~Over_UI_Protection
- U13 pad 1: /PWM GEN/~PWM_FREEWHEEL -> /~INT_PWM_Freewheel
- U13 pad 7: /PWM GEN/PWM_POWER -> /INT_PWM_Power
- U2 pad 1: Net-(Q1-Pad1) -> /PROGRAMMABLE BREAKER/S
- U2 pad 7: Net-(Q1-Pad1) -> /PROGRAMMABLE BREAKER/S
- U5 pad 15: (no net) -> /PWM
- U5 pad 4: (no net) -> /~PWM
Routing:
- net Net-(U4-Pad10): track 0.00 -> 11.9 mm
- net Net-(C2-Pad1): track 0.00 -> 10.7 mm
- net Net-(C9-Pad2): track 0.00 -> 7.62 mm
- net Net-(C7-Pad2): track 0.00 -> 7.62 mm
- net /PWM GEN/Ramp: track 0.00 -> 7.40 mm
- net /DRIVER COMMAND/Driver_LS: track 0.00 -> 7.10 mm
- net /Mode: track 0.00 -> 6.56 mm
- net /DRIVER COMMAND/Driver_RS: track 0.00 -> 6.42 mm
- net Net-(U4-Pad13): track 0.00 -> 5.93 mm
- net Net-(U4-Pad12): track 0.00 -> 5.93 mm
- net Net-(R30-Pad2): track 0.00 -> 5.86 mm
- net Net-(R29-Pad2): track 0.00 -> 5.03 mm
- net Net-(R33-Pad1): track 0.00 -> 4.51 mm
- net /DRIVER COMMAND/Driver_LP: track 0.00 -> 4.51 mm
- net Net-(R34-Pad1): track 0.00 -> 4.24 mm
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- added copper zone on F.Cu, net GND
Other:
- board outline added: 160 x 100 mm
- board text added: "Driver L"
- board text added: "Driver R"
- board text added: "Feedback"
- board text added: "PWM Gen."
- board text added: "Power supply"
- board text added: "Prog. breaker"
- board text added: "Ramp"
- board text added: "outline en mm placement des composants en 1.27 160x100"

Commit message: added footprint for sepic coil + no more errors in netlist
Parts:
- added C32: CP, Capacitor_SMD:C_Elec_4x5.8, F.Cu at (-214.7, 89.7)
- added L1: L_Core_Ferrite_Coupled_2_Parts, Sesame_footprint:WE-DD_1260_128012, F.Cu at (-214.7, 75.7)
- added R27: 47k, Sesame_footprint:R_0805_2012Metric_Pad1.20x1.40mm_HandSolder, F.Cu at (-166.1, 137.9)
- C1, C10, C11, C12, C13, C14, C15, C16, C17, C18, C19, C2, C20, C21, C22, C23, C24, C25, C26, C27, C28, C29, C3, C31, C33, C34, C35, C39, C4, C40, C41, C42, C43, C44, C45, C46, C5, C6, C7, C8, C9: footprint Capacitor_SMD:C_0805_2012Metric_Pad1.15x1.40mm_HandSolder -> Sesame_footprint:C_0805_2012Metric_Pad1.18x1.45mm_HandSolder
- J9: footprint Connector_PinHeader_2.54mm:PinHeader_2x16_P2.54mm_Vertical -> Connector_PinSocket_2.54mm:PinSocket_2x16_P2.54mm_Vertical
- R1, R10, R11, R12, R13, R14, R15, R16, R17, R18, R19, R2, R20, R21, R22, R23, R24, R25, R26, R29, R3, R30, R31, R32, R33, R34, R35, R36, R37, R38, R39, R4, R40, R41, R42, R43, R44, R45, R46, R47, R48, R49, R5, R50, R51, R52, R53, R54, R55, R56, R57, R58, R59, R6, R60, R61, R62, R63, R64, R65, R66, R67, R68, R69, R7, R70, R71, R72, R73, R74, R75, R76, R77, R78, R79, R8, R80, R81, R82, R83, R84, R85, R86, R87, R88, R89, R9, R90, R91, R92, R93, R94, R95, R96: footprint Resistor_SMD:R_0805_2012Metric_Pad1.15x1.40mm_HandSolder -> Sesame_footprint:R_0805_2012Metric_Pad1.20x1.40mm_HandSolder
- moved C16 397.9 mm to (-144.1, 196.2)
- moved R29 397.9 mm to (-116.8, 208.3)
- moved R30 397.9 mm to (-116.8, 198.8)
- moved R33 397.9 mm to (-116.8, 201.9)
- moved R34 397.9 mm to (-116.8, 205.1)
- moved TP11 397.9 mm to (-93.3, 205.7)
- moved TP13 397.9 mm to (-101.5, 216.4)
- moved TP15 397.9 mm to (-96.8, 213.6)
- moved TP16 397.9 mm to (-106.5, 219.3)
- moved TP17 397.9 mm to (-111.2, 220.8)
- moved U5 397.9 mm to (-144.1, 203.8)
- moved C12 397.9 mm to (-168.9, 217.2)
- moved C13 397.9 mm to (-144.8, 178.4)
- moved C15 397.9 mm to (-125.1, 196.2)
- moved R31 397.9 mm to (-133.3, 198.8)
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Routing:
- net /MOS DRIVER L/VS: track 0.00 -> 14.4 mm
- net /MOS DRIVER R/VS: track 0.00 -> 14.2 mm

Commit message: added footprint sepic + place place place
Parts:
- U15: footprint Package_SO:MSOP-16-1EP_3x4mm_P0.5mm_EP1.65x2.85mm_ThermalVias -> Sesame_footprint:MSE-16-1EP_3x4mm_P0.5mm_EP1.65x2.85mm_ThermalVias
- moved D12 334.9 mm to (132.1, 168.4)
- moved C12 292.4 mm to (123.2, 203.2)
- moved U3 292.4 mm to (123.2, 210.8)
- moved C15 194.3 mm to (69.2, 194.9)
- moved C16 194.3 mm to (50.2, 194.9)
- moved R29 194.3 mm to (77.5, 207.0)
- moved R30 194.3 mm to (77.5, 197.5)
- moved R31 194.3 mm to (61.0, 197.5)
- moved R32 194.3 mm to (61.0, 207.0)
- moved R33 194.3 mm to (77.5, 200.7)
- moved R34 194.3 mm to (77.5, 203.8)
- moved R35 194.3 mm to (61.0, 200.7)
- moved R36 194.3 mm to (61.0, 203.8)
- moved TP10 194.3 mm to (97.2, 216.7)
- moved TP11 194.3 mm to (101.0, 204.5)
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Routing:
- net /MOS DRIVER L/VS: track 14.4 -> 0.00 mm
- net /MOS DRIVER R/VS: track 14.2 -> 0.00 mm
- added copper zone on F.Cu, net /DC/DC CONVERTER/VD_LS
- added copper zone on F.Cu, net /L
- added copper zone on F.Cu, net /MOS DRIVER L/VS
- added copper zone on F.Cu, net /VProt_Left
- added copper zone on F.Cu, net Net-(D2-Pad1)
- removed copper zone on F.Cu, net GND
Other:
- board text added: "ALEEA 2021"
- board text added: "Ref"
- board text added: "Sepic sa mere"
